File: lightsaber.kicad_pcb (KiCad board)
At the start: 2 copper layers, 31.5 x 126.2 mm, 11 parts, among them SW1 Button, SW2 POWER, U1 C3 Pico

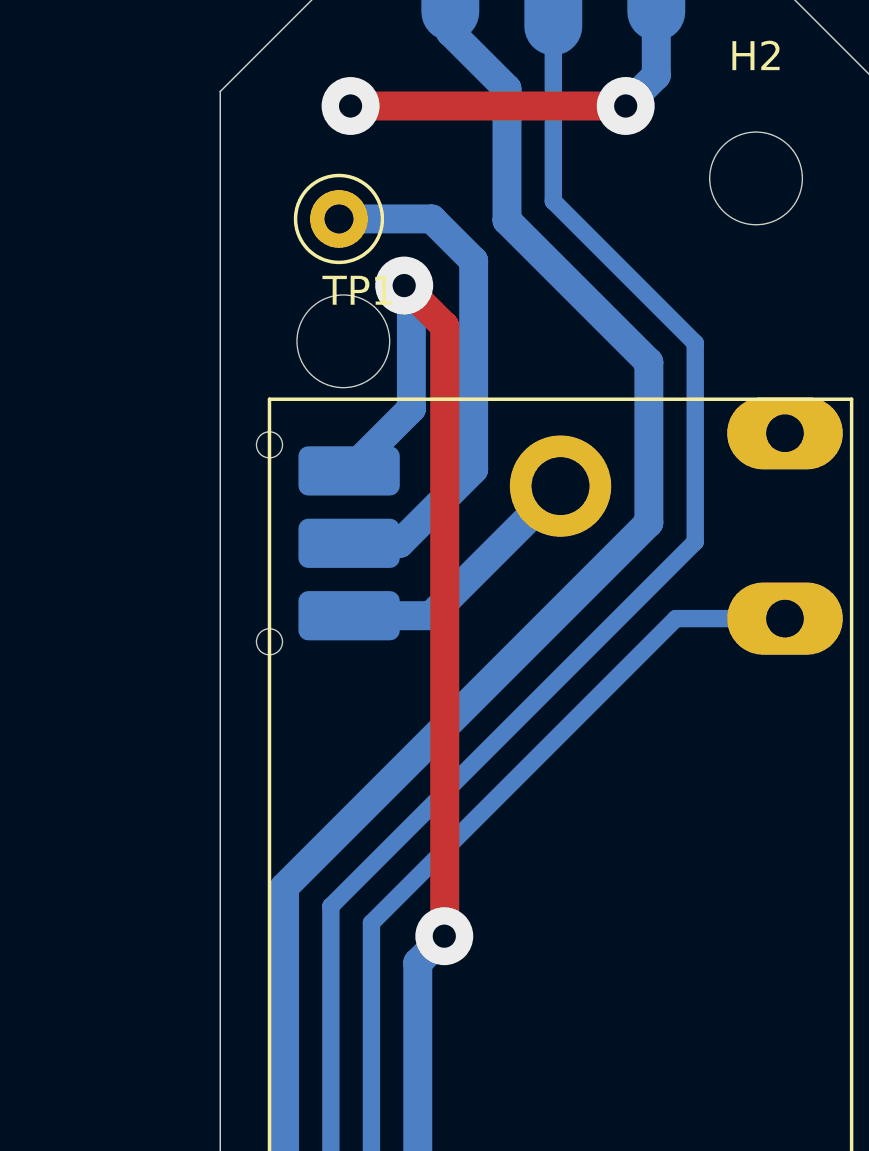
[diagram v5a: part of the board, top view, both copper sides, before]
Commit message: Reverse the polarity of the slide switch
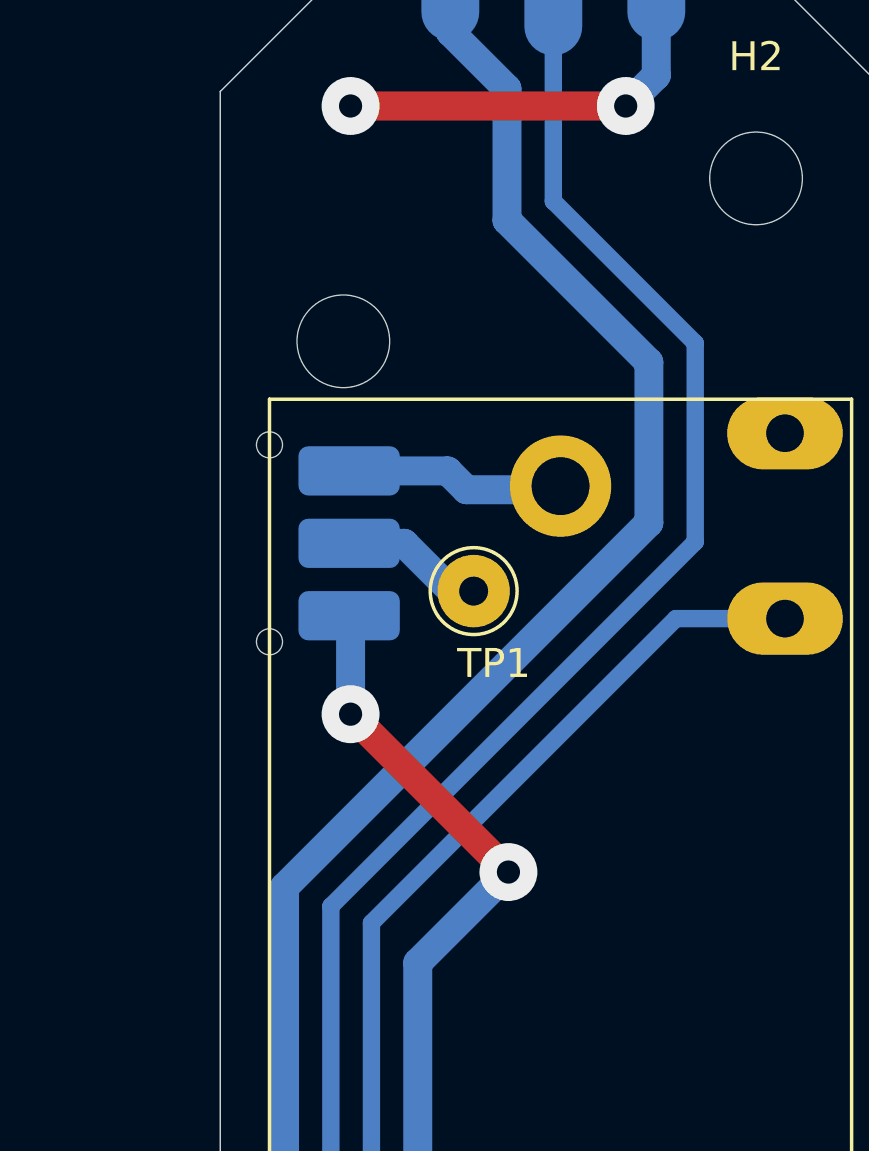
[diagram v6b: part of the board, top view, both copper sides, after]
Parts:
- moved TP1 13.7 mm to (117.8, 61.5)
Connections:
- SW2 pad 1: VBAT -> +5V
- SW2 pad 3: +5V -> VBAT
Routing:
- net +5V: track 126.7 -> 110.5 mm
- net +4V: track 17.8 -> 4.98 mm
- net VBAT: track 9.15 -> 7.62 mm
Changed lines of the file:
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@@
 	(footprint "TestPoint:TestPoint_Loop_D2.50mm_Drill1.0mm"
 		(layer "F.Cu")
-		(at 113.1 48.65)
+		(at 117.75 61.5)
 		(descr "wire loop as test point, loop diameter 2.5mm, hole diameter 1.0mm")
 		(tags "test point wire loop bead")
@@
 		(pad "1" thru_hole circle
 			(at 0 0)
-			(size 2 2)
+			(size 2.5 2.5)
 			(drill 1)
 			(layers "*.Cu" "*.Mask")
@@
 			(layers "B.Cu" "B.Paste" "B.Mask")
 			(roundrect_rratio 0.2)
-			(net 18 "VBAT")
+			(net 13 "+5V")
 			(pinfunction "A")
 			(pintype "passive")
@@
 			(layers "B.Cu" "B.Paste" "B.Mask")
 			(roundrect_rratio 0.2)
-			(net 13 "+5V")
+			(net 18 "VBAT")
 			(pinfunction "C")
 			(pintype "passive")
@@
 	)
 	(segment
-		(start 116.304327 48.65)
-		(end 117.75 50.095673)
+		(start 117 61.5)
+		(end 115.35 59.85)
 		(width 1)
 		(layer "B.Cu")
@@
 	)
 	(segment
-		(start 117.75 50.095673)
-		(end 117.75 57.3)
+		(start 115.35 59.85)
+		(end 113.45 59.85)
 		(width 1)
 		(layer "B.Cu")
@@
 	)
 	(segment
-		(start 113.1 48.65)
-		(end 116.304327 48.65)
-		(width 1)
-		(layer "B.Cu")
-		(net 3)
-	)
-	(segment
-		(start 117.75 57.3)
-		(end 115.2 59.85)
-		(width 1)
-		(layer "B.Cu")
-		(net 3)
-	)
-	(segment
-		(start 115.2 59.85)
-		(end 113.45 59.85)
+		(start 117.75 61.5)
+		(end 117 61.5)
 		(width 1)
 		(layer "B.Cu")
@@
 	)
 	(segment
-		(start 116.735421 73.415421)
-		(end 116.75 73.400842)
+		(start 118.950421 71.200421)
+		(end 113.5 65.75)
 		(width 1)
 		(layer "F.Cu")
 		(net 13)
 	)
-	(segment
-		(start 116.75 52.348365)
-		(end 115.351635 50.95)
-		(width 1)
-		(layer "F.Cu")
-		(net 13)
-	)
-	(segment
-		(start 116.75 73.400842)
-		(end 116.75 52.348365)
-		(width 1)
-		(layer "F.Cu")
-		(net 13)
-	)
 	(via
-		(at 116.735421 73.415421)
+		(at 118.950421 71.200421)
 		(size 2)
 		(drill 0.8)
@@
 	)
 	(via
-		(at 115.351635 50.95)
+		(at 113.5 65.75)
 		(size 2)
 		(drill 0.8)
@@
 	)
 	(segment
+		(start 118.62 151.87)
+		(end 125.68 158.93)
+		(width 1)
+		(layer "B.Cu")
+		(net 13)
+	)
+	(segment
+		(start 115.82 131.57)
+		(end 118.62 134.37)
+		(width 1)
+		(layer "B.Cu")
+		(net 13)
+	)
+	(segment
+		(start 113.5 62.4)
+		(end 113.45 62.35)
+		(width 1)
+		(layer "B.Cu")
+		(net 13)
+	)
+	(segment
+		(start 113.5 65.75)
+		(end 113.5 62.4)
+		(width 1)
+		(layer "B.Cu")
+		(net 13)
+	)
+	(segment
+		(start 118.62 134.37)
+		(end 118.62 151.87)
+		(width 1)
+		(layer "B.Cu")
+		(net 13)
+	)
+	(segment
 		(start 125.68 158.93)
 		(end 131.93 158.93)
@@
 	)
 	(segment
-		(start 118.62 134.37)
-		(end 118.62 151.87)
-		(width 1)
-		(layer "B.Cu")
-		(net 13)
-	)
-	(segment
-		(start 115.6 51.198365)
-		(end 115.351635 50.95)
-		(width 1)
-		(layer "B.Cu")
-		(net 13)
-	)
-	(segment
-		(start 115.82 131.57)
-		(end 118.62 134.37)
-		(width 1)
-		(layer "B.Cu")
-		(net 13)
-	)
-	(segment
-		(start 115.6 55.2)
-		(end 115.6 51.198365)
-		(width 1)
-		(layer "B.Cu")
-		(net 13)
-	)
-	(segment
-		(start 118.62 151.87)
-		(end 125.68 158.93)
+		(start 118.950421 71.200421)
+		(end 115.82 74.330842)
 		(width 1)
 		(layer "B.Cu")
@@
 		(start 115.82 74.330842)
 		(end 115.82 131.57)
-		(width 1)
-		(layer "B.Cu")
-		(net 13)
-	)
-	(segment
-		(start 116.735421 73.415421)
-		(end 115.82 74.330842)
-		(width 1)
-		(layer "B.Cu")
-		(net 13)
-	)
-	(segment
-		(start 113.45 57.35)
-		(end 115.6 55.2)
 		(width 1)
 		(layer "B.Cu")
@@
 	)
 	(segment
-		(start 113.45 62.35)
-		(end 116.275 62.35)
+		(start 113.45 57.35)
+		(end 116.85 57.35)
 		(width 1)
 		(layer "B.Cu")
@@
 	)
 	(segment
-		(start 116.275 62.35)
+		(start 117.5 58)
+		(end 120.625 58)
+		(width 1)
+		(layer "B.Cu")
+		(net 18)
+	)
+	(segment
+		(start 116.85 57.35)
+		(end 117.5 58)
+		(width 1)
+		(layer "B.Cu")
+		(net 18)
+	)
+	(segment
+		(start 120.625 58)
 		(end 120.75 57.875)
 		(width 1)

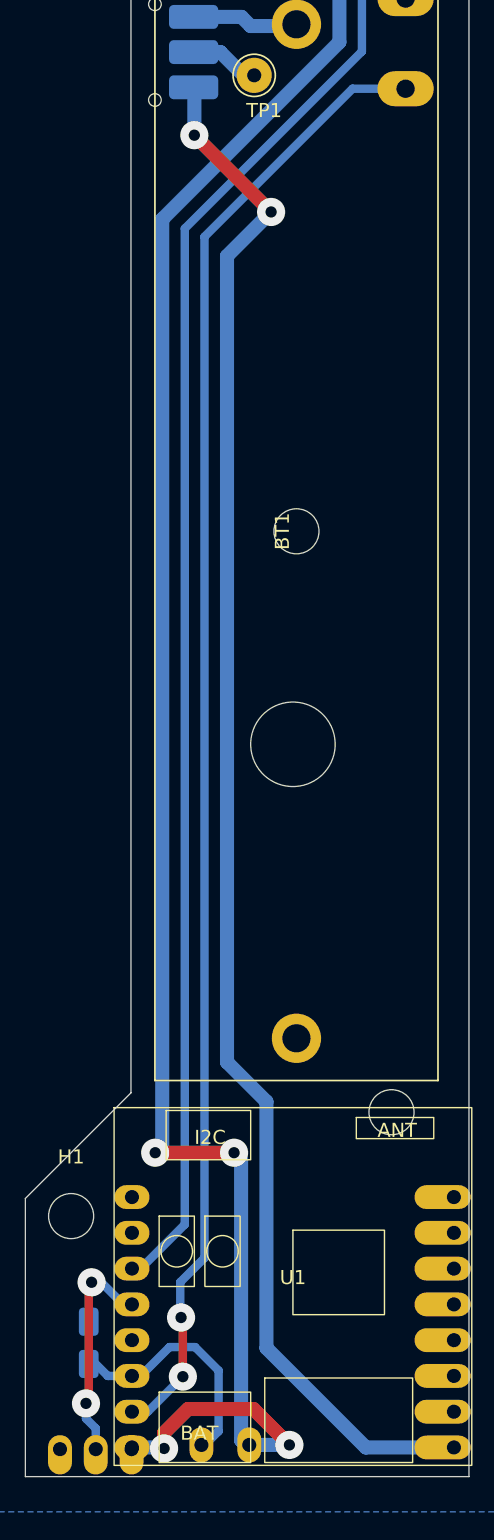
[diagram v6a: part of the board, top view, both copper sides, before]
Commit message: Denote the ADC pins
And change the pinout for the light sensor
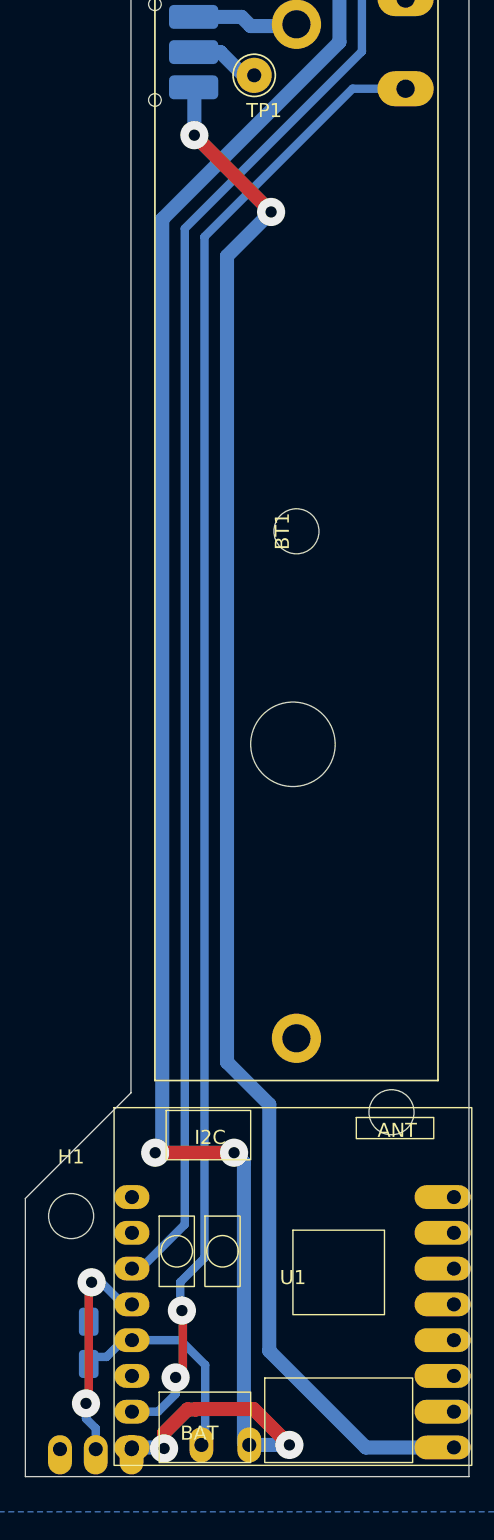
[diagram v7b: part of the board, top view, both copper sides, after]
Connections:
- U1 pad 11: Light -> unconnected-(U1-IO4/ADC/MOSI-Pad11)
- U1 pad 12: unconnected-(U1-IO0/MISO-Pad12) -> Light
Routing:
- net Light: track 17.4 -> 15.3 mm
